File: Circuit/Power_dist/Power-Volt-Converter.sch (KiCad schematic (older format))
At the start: 25 parts, among them P18 XT60, P19 XT60, P20 XT60, P21 XT60, P22 XT60, P23 XT60, P24 XT60, P25 XT60, Q8 BC817-40, U10 I6A24014A033V, U7 UWE-12/6-Q12P, U8 TEN_20-2411WIN, U9 TEN_20-2411WIN

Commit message: edit sch and add pcix16
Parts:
- removed C19: 100uF, Capacitors_SMD:CP_Elec_8x10.5, symbol C
- removed D13, D14: Led_Small, LEDs:LED_0603, symbol LED_Small
- removed P18, P19, P20, P21, P22, P23, P24, P25: XT60, Zeabus:XT60, symbol XT60
- removed R32, R33: 1k, Resistors_SMD:R_0603, symbol R
- removed R34: 2.2k, Resistors_SMD:R_0603, symbol R
- removed U10: I6A24014A033V, Zeabus:I6A24014A033V, symbol I6A24014A033V
- removed U9: TEN_20-2411WIN, Zeabus:TEN_20WIN, symbol TEN_20-2411WIN
- Q8: symbol BC817-40 -> BC847B
- U7: footprint Zeabus:UWE-xxxx -> zeabus:UWE-xxxx
- U8: footprint Zeabus:TEN_20WIN -> zeabus:TEN_20WIN
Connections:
- net GNDREF: now reaches D11.1 (K), U7.4 (-Vout)
- net GNDREF: now also D12.1 (K), U8.5 (-Vout)
- net +12V: now reaches R30.2, U7.8 (+Vout)
- net +5V: now reaches R31.2, U8.3 (+Vout)
- no-connect marks 4 -> 3
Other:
- note removed: "DSP"
- note removed: "DSP Supply"
- note removed: "Eth Switch"
- note removed: "Lamp1"
- note removed: "Lamp2"
- note removed: "NUC1"
- note removed: "NUC2"
- note removed: "Solenoid"
- note removed: "USB Hub"
- moved on the sheet: D12, R31, U8

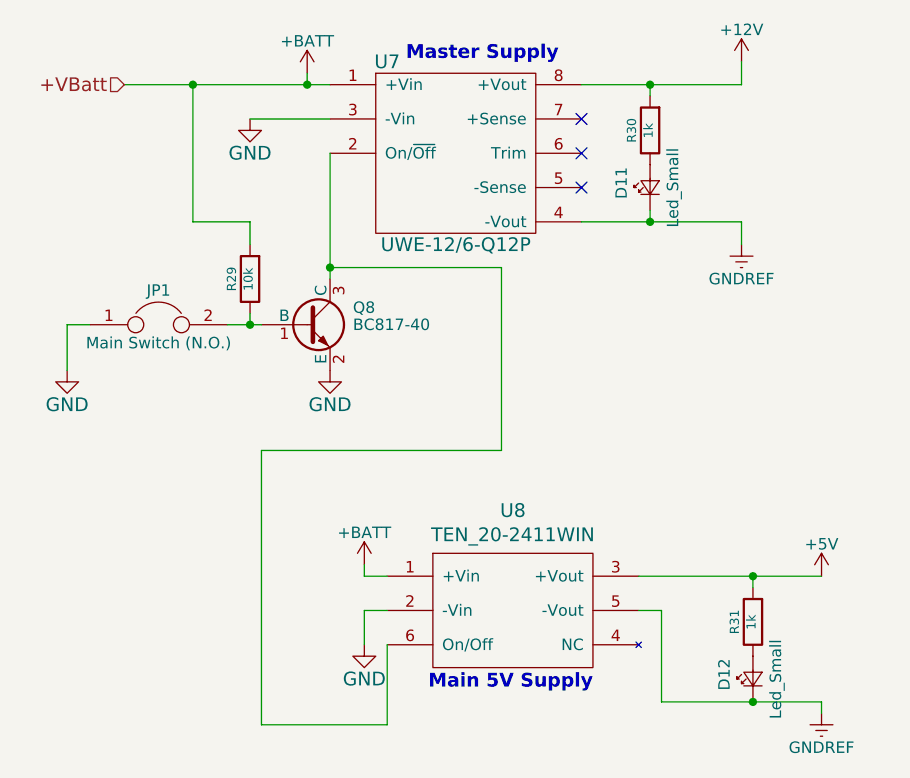
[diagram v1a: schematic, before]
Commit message: delete fuses at thrusters and oring + add power on jumper
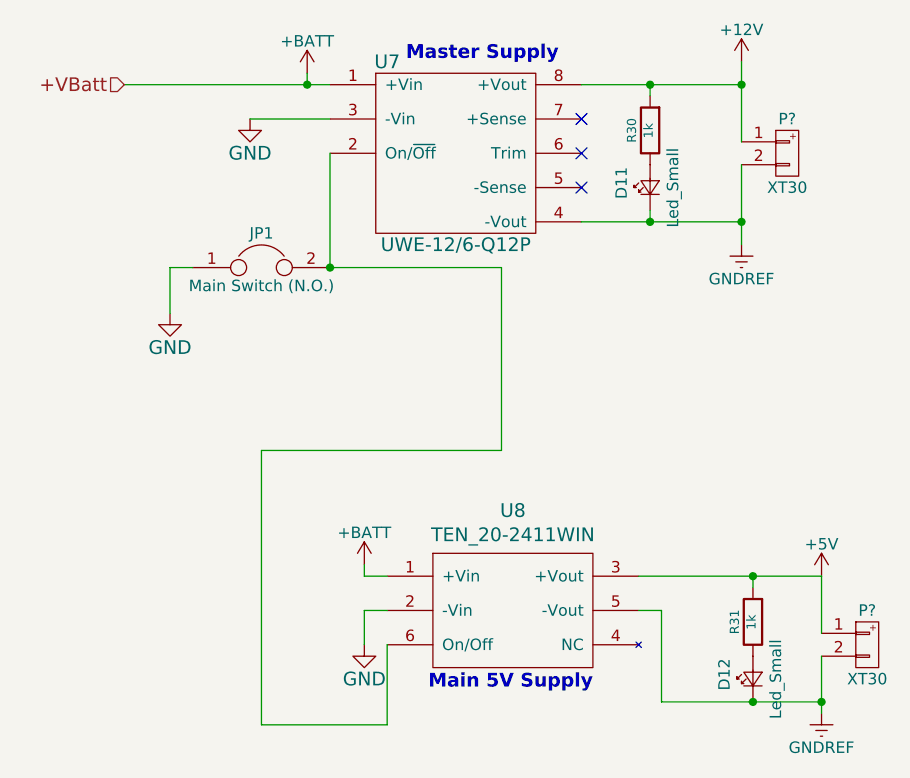
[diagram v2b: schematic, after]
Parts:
- removed Q8: BC817-40, TO_SOT_Packages_SMD:SOT-23, symbol BC847B
- removed R29: 10k, Resistors_SMD:R_0603, symbol R
- added P? (x2): XT30, symbol XT30
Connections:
- net +12V: now also P?.1 (P1)
- net +5V: now also P?.1 (P1)
- net GNDREF: now also P?.2 (P2), P?.2 (P2)
- net at JP1.2: now also U7.2 (On/~Off), U8.6 (On/Off)
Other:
- moved on the sheet: JP1
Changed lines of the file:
@@
 $Descr A4 11693 8268
 encoding utf-8
-Sheet 8 9
+Sheet 7 8
 Title "Power Voltage Convertor"
 Date "2017-04-06"
@@
 $EndComp
 $Comp
-L BC847B Q8
-U 1 1 58C81AD3
-P 2500 2500
-F 0 "Q8" H 2700 2575 50  0000 L CNN
-F 1 "BC817-40" H 2700 2500 50  0000 L CNN
-F 2 "TO_SOT_Packages_SMD:SOT-23" H 2700 2425 50  0001 L CIN
-F 3 "" H 2500 2500 50  0000 L CNN
-	1    2500 2500
-	1    0    0    -1
-$EndComp
-$Comp
 L Jumper JP1
 U 1 1 58C8A24F
-P 1850 2500
-F 0 "JP1" H 1850 2650 50  0000 C CNN
-F 1 "Main Switch (N.O.)" H 1850 2420 50  0000 C CNN
-F 2 "Pin_Headers:Pin_Header_Straight_1x02_Pitch2.54mm" H 1850 2500 60  0001 C CNN
-F 3 "" H 1850 2500 60  0000 C CNN
-	1    1850 2500
-	1    0    0    -1
-$EndComp
-$Comp
-L GND #PWR032
-U 1 1 58C8A79D
-P 2600 2700
-F 0 "#PWR032" H 2600 2450 60  0001 C CNN
-F 1 "GND" H 2600 2550 60  0000 C CNN
-F 2 "" H 2600 2700 60  0000 C CNN
-F 3 "" H 2600 2700 60  0000 C CNN
-	1    2600 2700
-	1    0    0    -1
-$EndComp
-$Comp
-L R R29
-U 1 1 58C8A817
-P 2250 2300
-F 0 "R29" V 2330 2300 40  0000 C CNN
-F 1 "10k" V 2257 2301 40  0000 C CNN
-F 2 "Resistors_SMD:R_0603" V 2180 2300 30  0001 C CNN
-F 3 "" H 2250 2300 30  0000 C CNN
-	1    2250 2300
-	-1   0    0    1
+P 2300 2250
+F 0 "JP1" H 2300 2400 50  0000 C CNN
+F 1 "Main Switch (N.O.)" H 2300 2170 50  0000 C CNN
+F 2 "Pin_Headers:Pin_Header_Straight_1x02_Pitch2.54mm" H 2300 2250 60  0001 C CNN
+F 3 "" H 2300 2250 60  0000 C CNN
+	1    2300 2250
+	1    0    0    -1
 $EndComp
 $Comp
 L GND #PWR033
 U 1 1 58C8B273
-P 1450 2700
-F 0 "#PWR033" H 1450 2450 60  0001 C CNN
-F 1 "GND" H 1450 2550 60  0000 C CNN
-F 2 "" H 1450 2700 60  0000 C CNN
-F 3 "" H 1450 2700 60  0000 C CNN
-	1    1450 2700
+P 1900 2450
+F 0 "#PWR033" H 1900 2200 60  0001 C CNN
+F 1 "GND" H 1900 2300 60  0000 C CNN
+F 2 "" H 1900 2450 60  0000 C CNN
+F 3 "" H 1900 2450 60  0000 C CNN
+	1    1900 2450
 	1    0    0    -1
 $EndComp
@@
 	2750 3600 2750 3550
 Wire Wire Line
-	2600 1750 2600 2300
-Wire Wire Line
-	2150 2500 2300 2500
-Wire Wire Line
-	2250 2450 2250 2500
-Connection ~ 2250 2500
-Wire Wire Line
-	2250 2050 2250 2150
-Wire Wire Line
-	1550 2500 1450 2500
-Wire Wire Line
-	1450 2500 1450 2700
+	2000 2250 1900 2250
+Wire Wire Line
+	1900 2250 1900 2450
 Connection ~ 2500 1450
-Wire Wire Line
-	2250 2050 2000 2050
-Wire Wire Line
-	2000 2050 2000 1450
-Connection ~ 2000 1450
 Wire Wire Line
 	2600 2250 3350 2250
@@
 NoConn ~ 3700 1900
 Wire Wire Line
-	4400 1450 4400 1350
-Wire Wire Line
-	4400 2050 4400 2150
+	4400 1350 4400 1700
+Wire Wire Line
+	4400 1800 4400 2150
 $Comp
 L +12V #PWR035
@@
 $EndComp
 Wire Wire Line
-	4750 4150 4750 4200
+	4750 3950 4750 4200
 $Comp
 L GNDREF #PWR037
@@
 	1    0    0    -1
 $EndComp
+Wire Wire Line
+	2600 1750 2600 2250
+$Comp
+L XT30 P?
+U 1 1 5A3A2D2C
+P 4600 1750
+F 0 "P?" H 4600 1900 50  0000 C CNN
+F 1 "XT30" H 4600 1600 50  0000 C CNN
+F 2 "" H 4600 1750 60  0000 C CNN
+F 3 "" H 4600 1750 60  0000 C CNN
+	1    4600 1750
+	1    0    0    -1
+$EndComp
+Connection ~ 4400 1450
+Connection ~ 4400 2050
+$Comp
+L XT30 P?
+U 1 1 5A3A2E02
+P 4950 3900
+F 0 "P?" H 4950 4050 50  0000 C CNN
+F 1 "XT30" H 4950 3750 50  0000 C CNN
+F 2 "" H 4950 3900 60  0000 C CNN
+F 3 "" H 4950 3900 60  0000 C CNN
+	1    4950 3900
+	1    0    0    -1
+$EndComp
+Wire Wire Line
+	4750 3600 4750 3850
+Connection ~ 4750 4150
 $EndSCHEMATC

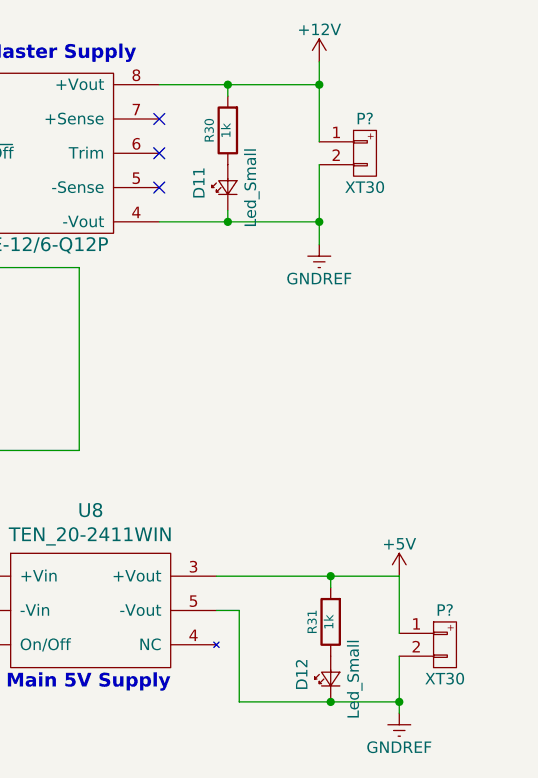
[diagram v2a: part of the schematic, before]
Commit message: component alignment on pcb
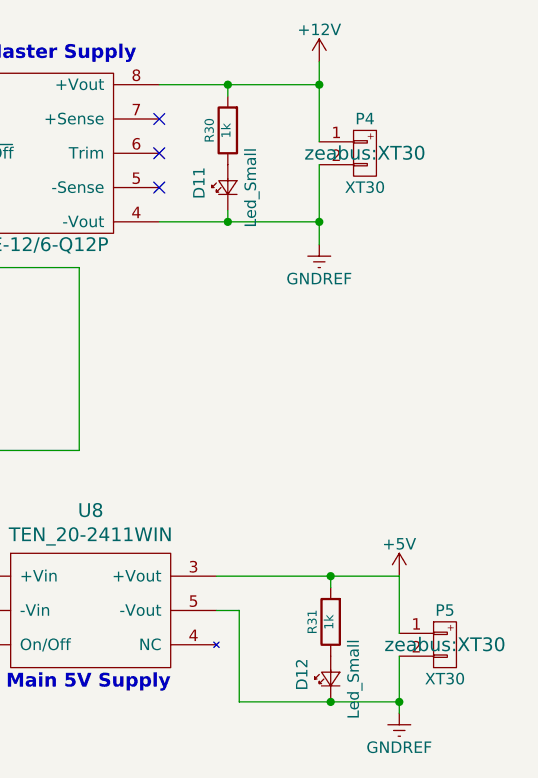
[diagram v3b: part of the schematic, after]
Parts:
- D11, D12: footprint LEDs:LED_0603 -> LEDs:LED_0603_HandSoldering
- P4, P5: renamed from P?; footprint (none) -> zeabus:XT30
- R30, R31: footprint Resistors_SMD:R_0603 -> Resistors_SMD:R_0603_HandSoldering
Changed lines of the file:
@@
 $EndDescr
 $Comp
-L GND #PWR029
+L GND #PWR037
 U 1 1 58C8506B
 P 2250 1600
-F 0 "#PWR029" H 2250 1350 60  0001 C CNN
+F 0 "#PWR037" H 2250 1350 60  0001 C CNN
 F 1 "GND" H 2250 1450 60  0000 C CNN
 F 2 "" H 2250 1600 60  0000 C CNN
@@
 F 0 "R30" V 4080 1650 40  0000 C CNN
 F 1 "1k" V 4007 1651 40  0000 C CNN
-F 2 "Resistors_SMD:R_0603" V 3930 1650 30  0001 C CNN
+F 2 "Resistors_SMD:R_0603_HandSoldering" V 3930 1650 30  0001 C CNN
 F 3 "" H 4000 1650 30  0000 C CNN
 	1    4000 1650
@@
 F 0 "D11" H 3950 2025 50  0000 L CNN
 F 1 "Led_Small" H 3825 1800 50  0000 L CNN
-F 2 "LEDs:LED_0603" V 4000 1900 60  0001 C CNN
+F 2 "LEDs:LED_0603_HandSoldering" V 4000 1900 60  0001 C CNN
 F 3 "" V 4000 1900 60  0000 C CNN
 	1    4000 1900
@@
 F 0 "R31" V 4530 3800 40  0000 C CNN
 F 1 "1k" V 4457 3801 40  0000 C CNN
-F 2 "Resistors_SMD:R_0603" V 4380 3800 30  0001 C CNN
+F 2 "Resistors_SMD:R_0603_HandSoldering" V 4380 3800 30  0001 C CNN
 F 3 "" H 4450 3800 30  0000 C CNN
 	1    4450 3800
@@
 F 0 "D12" H 4400 4175 50  0000 L CNN
 F 1 "Led_Small" H 4275 3950 50  0000 L CNN
-F 2 "LEDs:LED_0603" V 4450 4050 60  0001 C CNN
+F 2 "LEDs:LED_0603_HandSoldering" V 4450 4050 60  0001 C CNN
 F 3 "" V 4450 4050 60  0000 C CNN
 	1    4450 4050
@@
 $EndComp
 $Comp
-L GND #PWR030
+L GND #PWR038
 U 1 1 58C8524E
 P 2750 3900
-F 0 "#PWR030" H 2750 3650 60  0001 C CNN
+F 0 "#PWR038" H 2750 3650 60  0001 C CNN
 F 1 "GND" H 2750 3750 60  0000 C CNN
 F 2 "" H 2750 3900 60  0000 C CNN
@@
 +VBatt
 $Comp
-L +BATT #PWR031
+L +BATT #PWR039
 U 1 1 58C81568
 P 2500 1400
-F 0 "#PWR031" H 2500 1250 50  0001 C CNN
+F 0 "#PWR039" H 2500 1250 50  0001 C CNN
 F 1 "+BATT" H 2500 1540 50  0000 C CNN
 F 2 "" H 2500 1400 50  0000 C CNN
@@
 $EndComp
 $Comp
-L GND #PWR033
+L GND #PWR040
 U 1 1 58C8B273
 P 1900 2450
-F 0 "#PWR033" H 1900 2200 60  0001 C CNN
+F 0 "#PWR040" H 1900 2200 60  0001 C CNN
 F 1 "GND" H 1900 2300 60  0000 C CNN
 F 2 "" H 1900 2450 60  0000 C CNN
@@
 Master Supply
 $Comp
-L +BATT #PWR034
+L +BATT #PWR041
 U 1 1 58C8C536
 P 2750 3550
-F 0 "#PWR034" H 2750 3400 50  0001 C CNN
+F 0 "#PWR041" H 2750 3400 50  0001 C CNN
 F 1 "+BATT" H 2750 3690 50  0000 C CNN
 F 2 "" H 2750 3550 50  0000 C CNN
@@
 	4400 1800 4400 2150
 $Comp
-L +12V #PWR035
+L +12V #PWR042
 U 1 1 5A370E35
 P 4400 1350
-F 0 "#PWR035" H 4400 1200 50  0001 C CNN
+F 0 "#PWR042" H 4400 1200 50  0001 C CNN
 F 1 "+12V" H 4400 1490 50  0000 C CNN
 F 2 "" H 4400 1350 50  0001 C CNN
@@
 $EndComp
 $Comp
-L +5V #PWR036
+L +5V #PWR043
 U 1 1 5A370FF9
 P 4750 3600
-F 0 "#PWR036" H 4750 3450 50  0001 C CNN
+F 0 "#PWR043" H 4750 3450 50  0001 C CNN
 F 1 "+5V" H 4750 3740 50  0000 C CNN
 F 2 "" H 4750 3600 50  0001 C CNN
@@
 	4750 3950 4750 4200
 $Comp
-L GNDREF #PWR037
+L GNDREF #PWR044
 U 1 1 5A373347
 P 4400 2150
-F 0 "#PWR037" H 4400 1900 50  0001 C CNN
+F 0 "#PWR044" H 4400 1900 50  0001 C CNN
 F 1 "GNDREF" H 4400 2000 50  0000 C CNN
 F 2 "" H 4400 2150 50  0001 C CNN
@@
 $EndComp
 $Comp
-L GNDREF #PWR038
+L GNDREF #PWR045
 U 1 1 5A37353E
 P 4750 4200
-F 0 "#PWR038" H 4750 3950 50  0001 C CNN
+F 0 "#PWR045" H 4750 3950 50  0001 C CNN
 F 1 "GNDREF" H 4750 4050 50  0000 C CNN
 F 2 "" H 4750 4200 50  0001 C CNN
@@
 	2600 1750 2600 2250
 $Comp
-L XT30 P?
+L XT30 P4
 U 1 1 5A3A2D2C
 P 4600 1750
-F 0 "P?" H 4600 1900 50  0000 C CNN
+F 0 "P4" H 4600 1900 50  0000 C CNN
 F 1 "XT30" H 4600 1600 50  0000 C CNN
-F 2 "" H 4600 1750 60  0000 C CNN
+F 2 "zeabus:XT30" H 4600 1750 60  0000 C CNN
 F 3 "" H 4600 1750 60  0000 C CNN
 	1    4600 1750
@@
 Connection ~ 4400 2050
 $Comp
-L XT30 P?
+L XT30 P5
 U 1 1 5A3A2E02
 P 4950 3900
-F 0 "P?" H 4950 4050 50  0000 C CNN
+F 0 "P5" H 4950 4050 50  0000 C CNN
 F 1 "XT30" H 4950 3750 50  0000 C CNN
-F 2 "" H 4950 3900 60  0000 C CNN
+F 2 "zeabus:XT30" H 4950 3900 60  0000 C CNN
 F 3 "" H 4950 3900 60  0000 C CNN
 	1    4950 3900
